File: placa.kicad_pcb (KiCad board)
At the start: 2 copper layers, 40 x 40 mm, 76 parts, among them J1 SW, J10 CONN_01X04_Straight, J12 CONN_01X04_Straight, J13 CONN_01X04_Straight, J14 CONN_01X04_Straight, J15 CONN_01X04_Straight, J16 CONN_01X04_Straight, J17 CONN_01X04_Straight, J18 CONN_01X06_Straight, J2 μUSB, J3 BATT, J5 CONN_01X04_Straight, J6 CONN_01X04_Straight, J7 CONN_02X12_Straight, J8 CONN_01X12_Straight, J9 CONN_01X04_Straight, Q1 FDC606P, Q2 BSS84, U1 AP2112K-3.3TRG1, U2 MCP73831, U3 MIC2253-06YML-TR, U4 ADS1000, U5 LMC7101AIM5, U6 DRV8837, U7 PCA9670, U8 DRV8837

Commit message: Schematic: Level shifter
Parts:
- removed J14, J15, J16, J17: CONN_01X04_Straight, Pin_Headers:Pin_Header_Straight_1x04_Pitch2.54mm
- removed J18: CONN_01X06_Straight, Pin_Headers:Pin_Header_Straight_1x06_Pitch2.54mm
- removed JP4: Jumper_NO, Connectors:GS2
- added Q3, Q4: BSS138P, TO_SOT_Packages_SMD:SOT-23, F.Cu at (168.5, 115.1)
- added R23, R24: 4.7k, Resistors_SMD:R_0402, F.Cu at (168.5, 115.1)
- D2: value BA340A -> LED; footprint Diodes_SMD:D_SMA -> LEDs:LED_0603
- D3: value LED -> BA340A; footprint LEDs:LED_0603 -> Diodes_SMD:D_SMA
- J11: value ~ -> CONN_01X04_Straight; footprint Connectors_Terminal_Blocks:TerminalBlock_Pheonix_MPT-2.54mm_2pol -> Pin_Headers:Pin_Header_Straight_1x04_Pitch2.54mm
- J5: value CONN_01X04_Straight -> ~; footprint Pin_Headers:Pin_Header_Straight_1x04_Pitch2.54mm -> Connectors_Terminal_Blocks:TerminalBlock_Pheonix_MPT-2.54mm_2pol
- J6: value CONN_01X04_Straight -> CONN_01X12_Straight; footprint Pin_Headers:Pin_Header_Straight_1x04_Pitch2.54mm -> Pin_Headers:Pin_Header_Straight_1x12_Pitch2.54mm
- J8: value CONN_01X12_Straight -> CONN_01X04_Straight; footprint Pin_Headers:Pin_Header_Straight_1x12_Pitch2.54mm -> Pin_Headers:Pin_Header_Straight_1x04_Pitch2.54mm
- R10: value 10k -> 620; footprint Resistors_SMD:R_0402 -> Resistors_SMD:R_0603
- R15: footprint Resistors_SMD:R_0603 -> Resistors_SMD:R_0402
- R16: value 0 -> 10k
- R17, R5: value 10k -> 0; footprint Resistors_SMD:R_0402 -> Resistors_SMD:R_0603
- R2: value 2k -> 330
- R20: value 4.7k -> 10k
- R21: value 330 -> 4.7k
- R3: value 30.9k -> 2k; footprint Resistors_SMD:R_0603 -> Resistors_SMD:R_0402
- R4: value 0 -> 30.9k
- R9: value 620 -> 10k; footprint Resistors_SMD:R_0603 -> Resistors_SMD:R_0402
- U7: value PCA9670 -> DRV8837; footprint alvaroferran:TSSOP-16 -> alvaroferran:WSON-8
- U8: value DRV8837 -> PCA9670; footprint alvaroferran:WSON-8 -> alvaroferran:TSSOP-16
- moved U8 82.9 mm to (172.2, 91.9), turned to 180 degrees
- moved J9 76.6 mm to (159.5, 77.0), turned to 180 degrees
- moved U6 50.5 mm to (179.3, 88.9), turned to 180 degrees
- moved J10 47.2 mm to (164.6, 77.0), turned to 180 degrees
- moved J5 37.4 mm to (185.2, 96.3), turned to 90 degrees
- moved J13 37.0 mm to (162.6, 98.0), turned to 180 degrees
- moved J12 36.8 mm to (159.8, 98.0), turned to 180 degrees
- moved J11 36.7 mm to (157.0, 98.0), turned to 180 degrees
- moved U7 28.1 mm to (179.3, 95.0), turned to 180 degrees
- moved J8 27.9 mm to (156.7, 77.0), turned to 180 degrees
- moved J3 22.9 mm to (170.2, 71.1)
- moved J6 20.2 mm to (182.5, 66.4), turned to 270 degrees
- moved J1 8.89 mm to (185.2, 80.0)
- moved J4 8.89 mm to (185.2, 90.2)
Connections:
- D1 pad 2: Net-(C5-Pad1) -> (no net)
- D2 pad 1: Net-(C7-Pad1) -> Net-(D2-Pad1)
- D2 pad 2: Net-(D2-Pad2) -> Net-(C5-Pad1)
- D3 pad 1: Net-(D3-Pad1) -> Net-(C7-Pad1)
- D3 pad 2: (no net) -> Net-(D3-Pad2)
- J10 pad 2: /UART2T -> /USB2+
- J10 pad 3: /UART2R -> /USB2-
- J11 pad 2: Net-(J11-Pad2) -> Net-(J11-Pad1)
- J12 pad 1: (no net) -> Net-(J12-Pad1)
- J12 pad 2: /SDA -> Net-(J12-Pad1)
- J12 pad 3: /SCL -> Net-(J12-Pad1)
- J12 pad 4: (no net) -> Net-(J12-Pad1)
- J13 pad 1: (no net) -> /GPIO0
- J13 pad 2: /SDA -> /GPIO1
- J13 pad 3: /SCL -> /GPIO2
- J13 pad 4: (no net) -> /GPIO3
- J5 pad 1: (no net) -> Net-(J5-Pad1)
- J5 pad 2: /USB1+ -> Net-(J5-Pad2)
- J6 pad 2: /USB2+ -> (no net)
- J6 pad 3: /USB2- -> (no net)
- J6 pad 4: (no net) -> /USB2+
- J7 pad 10: /UART1R -> (no net)
- J7 pad 11: /UART2T -> (no net)
- J7 pad 19: /MOSI -> (no net)
- J7 pad 21: /MISO -> (no net)
- J7 pad 22: /UART2R -> (no net)
- J7 pad 23: /SCK -> (no net)
- J7 pad 24: /CS -> (no net)
- J7 pad 8: /UART1T -> (no net)
- J8 pad 2: /USB1+ -> /SDA
- J8 pad 3: /USB1- -> /SCL
- J8 pad 4: /USB2+ -> (no net)
- J9 pad 2: /UART1T -> /SDA
- J9 pad 3: /UART1R -> /SCL
- L1 pad 2: Net-(D2-Pad2) -> Net-(D3-Pad2)
- R1 pad 1: Net-(R1-Pad1) -> (no net)
- R10 pad 1: Net-(R10-Pad1) -> Net-(C13-Pad1)
- R10 pad 2: (no net) -> Net-(R10-Pad2)
- R12 pad 1: /MOTEN -> Net-(R12-Pad1)
- R13 pad 1: Net-(R13-Pad1) -> /MOTEN
- R15 pad 1: Net-(C7-Pad2) -> Net-(R15-Pad1)
- R15 pad 2: GNDA -> (no net)
- R16 pad 1: (no net) -> Net-(C7-Pad2)
- R16 pad 2: GNDPWR -> GNDA
- R17 pad 1: Net-(JP1-Pad1) -> (no net)
- R17 pad 2: (no net) -> GNDPWR
- R18 pad 1: Net-(JP2-Pad1) -> Net-(JP1-Pad1)
- R19 pad 1: Net-(JP3-Pad1) -> Net-(JP2-Pad1)
- R2 pad 2: (no net) -> Net-(D2-Pad1)
- R20 pad 1: /SDA -> Net-(JP3-Pad1)
- R20 pad 2: Net-(JP4-Pad1) -> (no net)
- R21 pad 1: (no net) -> Net-(Q3-Pad1)
- R21 pad 2: Net-(D3-Pad1) -> /SDA
- R22 pad 1: /SCL -> (no net)
- R22 pad 2: Net-(JP4-Pad1) -> /SDAH
- R3 pad 1: Net-(C7-Pad1) -> Net-(R3-Pad1)
- R3 pad 2: Net-(C7-Pad2) -> (no net)
- R4 pad 1: (no net) -> Net-(C7-Pad1)
- R4 pad 2: GNDA -> Net-(C7-Pad2)
- R5 pad 2: Net-(R10-Pad1) -> GNDA
- R7 pad 2: Net-(R13-Pad1) -> Net-(R12-Pad1)
- R9 pad 1: Net-(C13-Pad1) -> (no net)
- R9 pad 2: Net-(R9-Pad2) -> Net-(R15-Pad1)
- U2 pad 1: Net-(R1-Pad1) -> Net-(R2-Pad1)
- U2 pad 5: Net-(R2-Pad1) -> Net-(R3-Pad1)
- U3 pad 12: Net-(R9-Pad2) -> Net-(R10-Pad2)
- U3 pad 7: Net-(D2-Pad2) -> Net-(D3-Pad2)
- U3 pad 8: Net-(D2-Pad2) -> Net-(D3-Pad2)
- U4 pad 1: Net-(R14-Pad1) -> Net-(R15-Pad1)
- U4 pad 6: Net-(R13-Pad1) -> Net-(R14-Pad1)
- U5 pad 3: Net-(R10-Pad1) -> Net-(R11-Pad1)
- U5 pad 4: Net-(R11-Pad1) -> Net-(R12-Pad1)
- U7 pad 1: Net-(JP3-Pad1) -> (no net)
- U7 pad 2: /GPIO0 -> Net-(J5-Pad1)
- U7 pad 3: /GPIO1 -> Net-(J5-Pad2)
- U7 pad 4: /GPIO2 -> (no net)
- U7 pad 5: /GPIO3 -> /MOT2B
- U7 pad 6: (no net) -> /MOT2A
- U7 pad 7: /MOT1A -> /MOTEN
- U7 pad 8: /MOT1B -> (no net)
- U7 pad 9: /MOT2A -> (no net)
- U8 pad 1: (no net) -> Net-(JP3-Pad1)
- U8 pad 2: Net-(J11-Pad1) -> /GPIO0
- U8 pad 3: Net-(J11-Pad2) -> /GPIO1
- U8 pad 4: (no net) -> /GPIO2
- U8 pad 5: /MOT2B -> /GPIO3
- U8 pad 6: /MOT2A -> (no net)
- U8 pad 7: /MOTEN -> /MOT1A
- U8 pad 8: (no net) -> /MOT1B
- U8 pad 9: (no net) -> /MOT2A

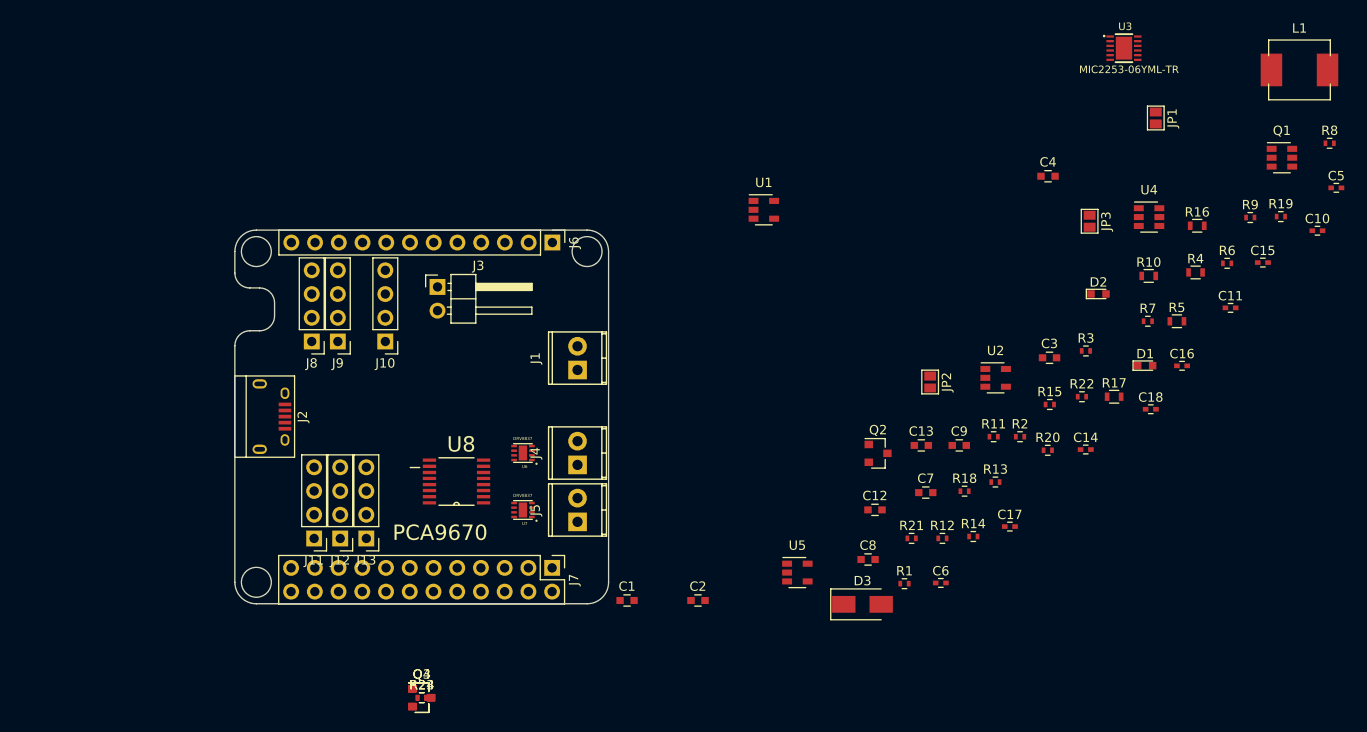
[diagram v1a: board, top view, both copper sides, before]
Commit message: Schematic: Protection diode
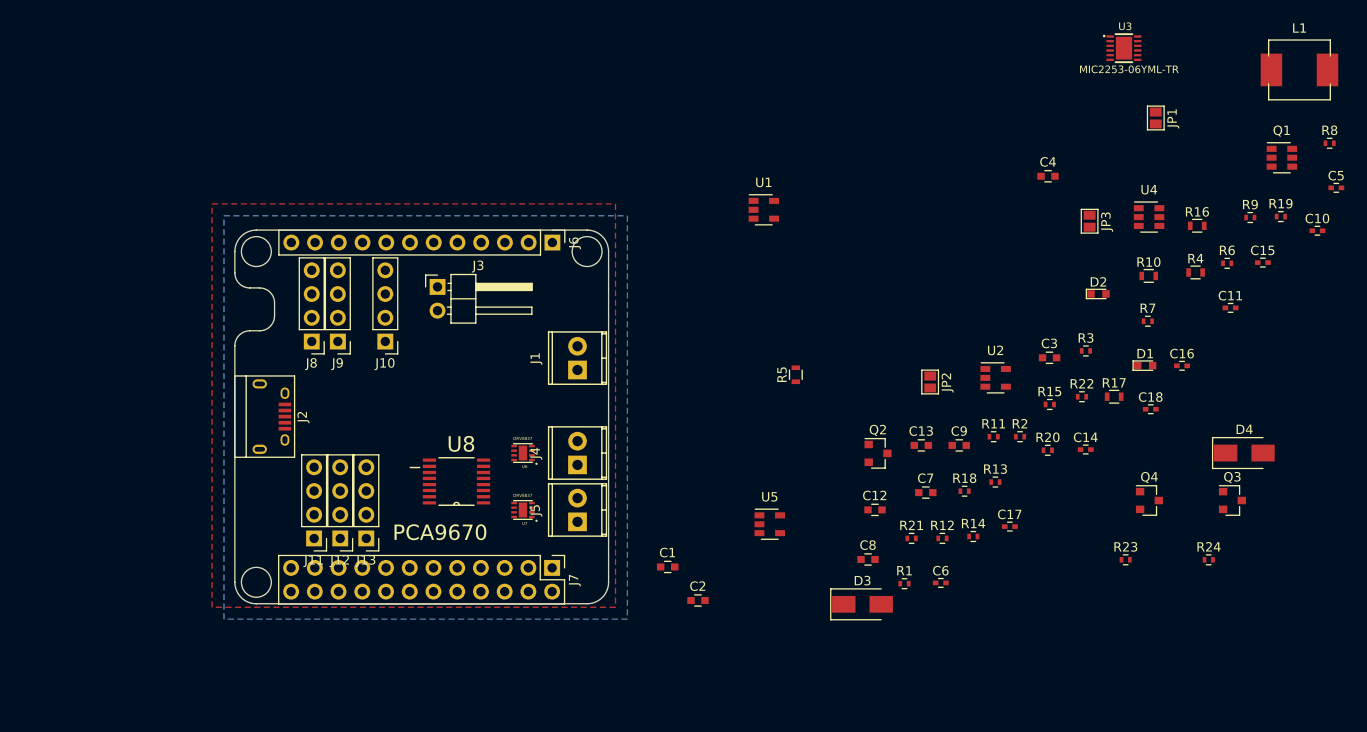
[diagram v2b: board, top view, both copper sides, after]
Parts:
- added D4: BA340A, Diodes_SMD:D_SMA, F.Cu at (256.5, 88.9)
- R16: value 10k -> 0
- R17: value 0 -> 10k
- R4: value 30.9k -> 0
- R5: value 0 -> 30.9k
- moved Q3 89.3 mm to (255.3, 94.0)
- moved R24 85.5 mm to (252.7, 100.3)
- moved Q4 80.7 mm to (246.4, 94.0)
- moved R23 76.8 mm to (243.8, 100.3)
- moved R5 41.2 mm to (208.5, 80.5), turned to 90 degrees
- moved U5 5.96 mm to (205.7, 96.5)
- moved C1 5.64 mm to (194.8, 101.1)
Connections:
- C1 pad 1: (no net) -> 5V
- C1 pad 2: (no net) -> GND
- C10 pad 1: (no net) -> 3.3V
- C10 pad 2: (no net) -> GND
- C11 pad 1: (no net) -> 3.3V
- C11 pad 2: (no net) -> GND
- C14 pad 1: (no net) -> 3.3V
- C14 pad 2: (no net) -> GND
- C15 pad 1: (no net) -> 5V
- C15 pad 2: (no net) -> GND
- C16 pad 1: (no net) -> 3.3V
- C16 pad 2: (no net) -> GND
- C17 pad 1: (no net) -> 5V
- C17 pad 2: (no net) -> GND
- C18 pad 1: (no net) -> 5V
- C18 pad 2: (no net) -> GND
- C2 pad 1: (no net) -> 3.3V
- C2 pad 2: (no net) -> GND
- C3 pad 1: Net-(C3-Pad1) -> 5V
- C3 pad 2: Net-(C3-Pad2) -> GND
- C4 pad 1: Net-(C4-Pad1) -> 3.3V
- C4 pad 2: Net-(C3-Pad2) -> GND
- C5 pad 2: (no net) -> GND
- C6 pad 2: (no net) -> GND
- C7 pad 1: Net-(C7-Pad1) -> 5V
- C8 pad 1: Net-(C8-Pad1) -> VBAT
- C9 pad 1: Net-(C7-Pad1) -> 5V
- D1 pad 2: (no net) -> 3.3V
- D3 pad 1: Net-(C7-Pad1) -> 5V
- J1 pad 1: (no net) -> VBAT
- J10 pad 1: (no net) -> 5V
- J10 pad 4: (no net) -> GND
- J11 pad 1: Net-(J11-Pad1) -> GND
- J11 pad 2: Net-(J11-Pad1) -> GND
- J11 pad 3: Net-(J11-Pad1) -> GND
- J11 pad 4: Net-(J11-Pad1) -> GND
- J12 pad 1: Net-(J12-Pad1) -> 5V
- J12 pad 2: Net-(J12-Pad1) -> 5V
- J12 pad 3: Net-(J12-Pad1) -> 5V
- J12 pad 4: Net-(J12-Pad1) -> 5V
- J2 pad 5: (no net) -> GND
- J3 pad 2: (no net) -> GND
- J6 pad 12: (no net) -> GND
- J7 pad 14: Net-(J7-Pad14) -> GND
- J7 pad 20: Net-(J7-Pad14) -> GND
- J7 pad 6: Net-(J7-Pad14) -> GND
- J7 pad 9: (no net) -> GND
- J8 pad 1: (no net) -> 3.3V
- J8 pad 4: (no net) -> GND
- J9 pad 1: (no net) -> 3.3V
- J9 pad 4: (no net) -> GND
- JP1 pad 2: Net-(JP1-Pad2) -> 5V
- JP2 pad 2: Net-(JP1-Pad2) -> 5V
- JP3 pad 2: Net-(JP1-Pad2) -> 5V
- L1 pad 1: Net-(C8-Pad1) -> VBAT
- Q1 pad 3: Net-(J3-Pad1) -> GND
- Q2 pad 2: (no net) -> 3.3V
- Q3 pad 1: Net-(Q3-Pad1) -> 3.3V
- Q4 pad 1: Net-(Q4-Pad1) -> 3.3V
- R1 pad 1: (no net) -> GND
- R11 pad 2: (no net) -> GND
- R12 pad 2: (no net) -> GND
- R13 pad 2: (no net) -> GND
- R14 pad 2: (no net) -> GND
- R15 pad 2: (no net) -> GND
- R16 pad 1: Net-(C7-Pad2) -> GND
- R16 pad 2: GNDA -> GNDPWR
- R17 pad 1: (no net) -> Net-(C7-Pad2)
- R17 pad 2: GNDPWR -> GNDA
- R18 pad 2: (no net) -> GND
- R19 pad 2: (no net) -> GND
- R20 pad 2: (no net) -> GND
- R21 pad 1: Net-(Q3-Pad1) -> 3.3V
- R22 pad 1: (no net) -> 5V
- R23 pad 1: Net-(Q4-Pad1) -> 3.3V
- R24 pad 1: (no net) -> 5V
- R3 pad 2: (no net) -> GND
- R4 pad 1: Net-(C7-Pad1) -> GND
- R4 pad 2: Net-(C7-Pad2) -> GNDA
- R5 pad 1: (no net) -> 5V
- R5 pad 2: GNDA -> Net-(C7-Pad2)
- R6 pad 1: (no net) -> 3.3V
- R7 pad 1: (no net) -> VBAT
- R8 pad 1: (no net) -> VBAT
- R9 pad 1: (no net) -> 3.3V
- U1 pad 1: Net-(C3-Pad1) -> 5V
- U1 pad 2: Net-(C3-Pad2) -> GND
- U1 pad 3: Net-(C3-Pad1) -> 5V
- U1 pad 5: Net-(C4-Pad1) -> 3.3V
- U2 pad 2: (no net) -> GND
- U3 pad 10: Net-(C8-Pad1) -> VBAT
- U3 pad 11: Net-(C8-Pad1) -> VBAT
- U3 pad 9: Net-(C7-Pad1) -> 5V
- U4 pad 2: (no net) -> GND
- U4 pad 5: (no net) -> 3.3V
- U5 pad 2: (no net) -> 3.3V
- U5 pad 5: (no net) -> GND
- U6 pad 1: (no net) -> 5V
- U6 pad 4: (no net) -> GND
- U6 pad 8: (no net) -> 3.3V
- U7 pad 1: (no net) -> 5V
- U7 pad 4: (no net) -> GND
- U7 pad 8: (no net) -> 3.3V
- U8 pad 11: Net-(JP1-Pad2) -> 5V
- U8 pad 14: Net-(JP1-Pad2) -> 5V
- U8 pad 6: (no net) -> GND
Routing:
- added copper zone on B.Cu, net GND
- added copper zone on F.Cu, net GND

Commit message: Schematic: Batt inv removed
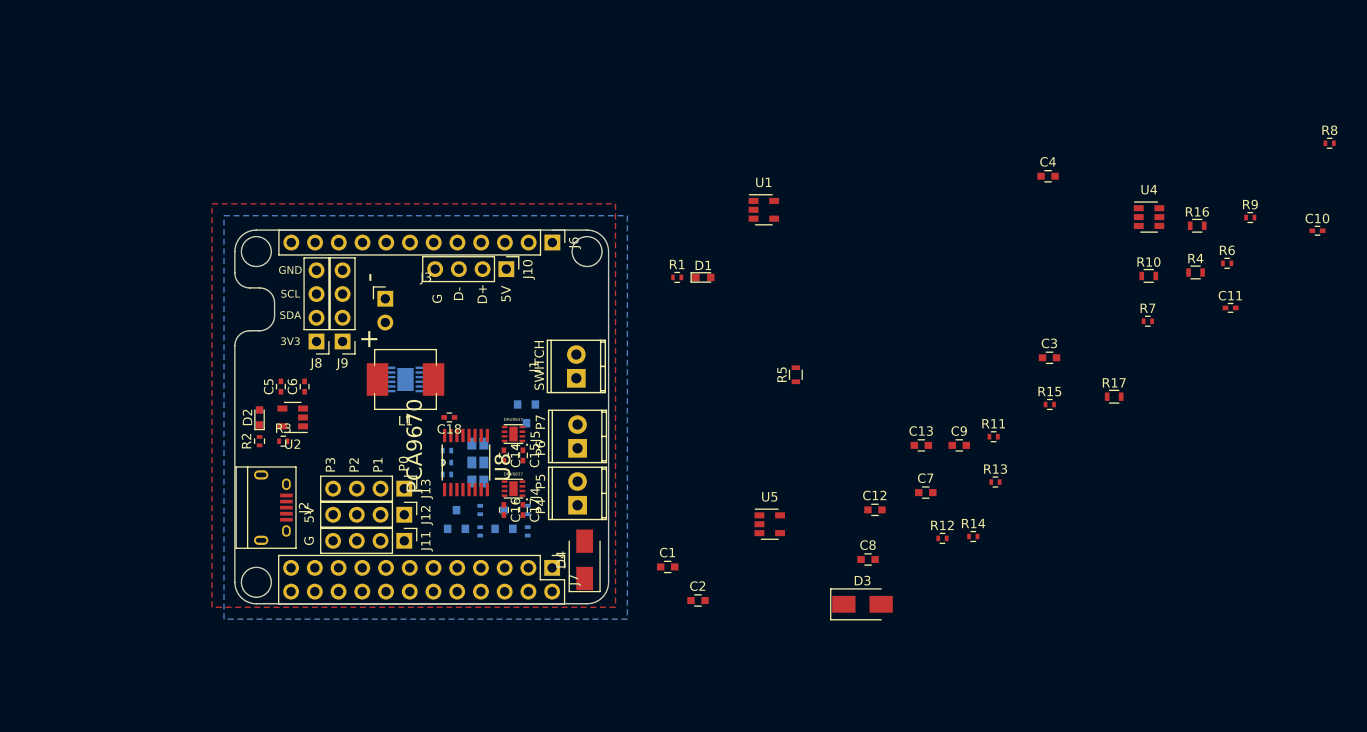
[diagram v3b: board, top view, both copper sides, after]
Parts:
- removed Q4: BSS138P, TO_SOT_Packages_SMD:SOT-23
- JP1, JP2, JP3, Q3, R18, R19, R20, R21, R22, R23, R24, U3: moved to B.Cu
- Q1: value FDC606P -> BSS84; footprint TO_SOT_Packages_SMD:SOT-23-6 -> TO_SOT_Packages_SMD:SOT-23; moved to B.Cu
- Q2: value BSS84 -> BSS138P; moved to B.Cu
- moved C5 115.0 mm to (153.4, 81.8), turned to 90 degrees
- moved L1 101.3 mm to (166.8, 81.0), turned to 180 degrees
- moved R19 93.0 mm to (171.2, 89.9), turned to 180 degrees
- moved D2 90.8 mm to (151.1, 85.1), turned to 90 degrees
- moved R3 86.5 mm to (153.7, 87.6)
- moved Q1 85.4 mm to (179.7, 84.7), turned to 270 degrees
- moved U3 84.7 mm to (166.8, 81.0)
- moved C15 81.8 mm to (179.3, 89.2), turned to 270 degrees
- moved R2 81.4 mm to (151.1, 87.6), turned to 90 degrees
- moved JP1 80.5 mm to (174.5, 87.9), turned to 270 degrees
- moved Q3 78.0 mm to (177.3, 96.0), turned to 90 degrees
- moved U2 75.3 mm to (154.7, 85.1), turned to 180 degrees
- moved C18 75.1 mm to (171.4, 85.1), turned to 180 degrees
- moved C16 74.2 mm to (177.3, 95.0), turned to 270 degrees
- moved R24 73.1 mm to (179.8, 95.0), turned to 270 degrees
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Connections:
- J3 pad 1: Net-(J3-Pad1) -> GND
- J3 pad 2: GND -> Net-(C6-Pad1)
- Q1 pad 1: Net-(J3-Pad1) -> Net-(Q1-Pad1)
- Q1 pad 2: Net-(J3-Pad1) -> 3.3V
- Q1 pad 3: GND -> /MOTEN
- Q2 pad 1: Net-(Q2-Pad1) -> 3.3V
- Q2 pad 2: 3.3V -> /SDA
- Q2 pad 3: /MOTEN -> /SDAH
- Q3 pad 2: /SDA -> /SCL
- Q3 pad 3: /SDAH -> /SCLH
- U5 pad 1: Net-(Q2-Pad1) -> Net-(Q1-Pad1)
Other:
- board text added: "+"
- board text added: "-"
- board text added: "3V3"
- board text added: "5V"
- board text added: "CHANGE BAT CONNECTOR ADD STRESS RELIEF FOR WIRES"
- board text added: "D+"
- board text added: "D-"
- board text added: "G"
- board text added: "GND"
- board text added: "P0"
- board text added: "P1"
- board text added: "P2"
- board text added: "P3"
- board text added: "P4"
- board text added: "P5"
- board text added: "P6"
- board text added: "P7"
- board text added: "SCL"
- board text added: "SDA"
- board text added: "SWITCH"

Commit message: Board: components in place
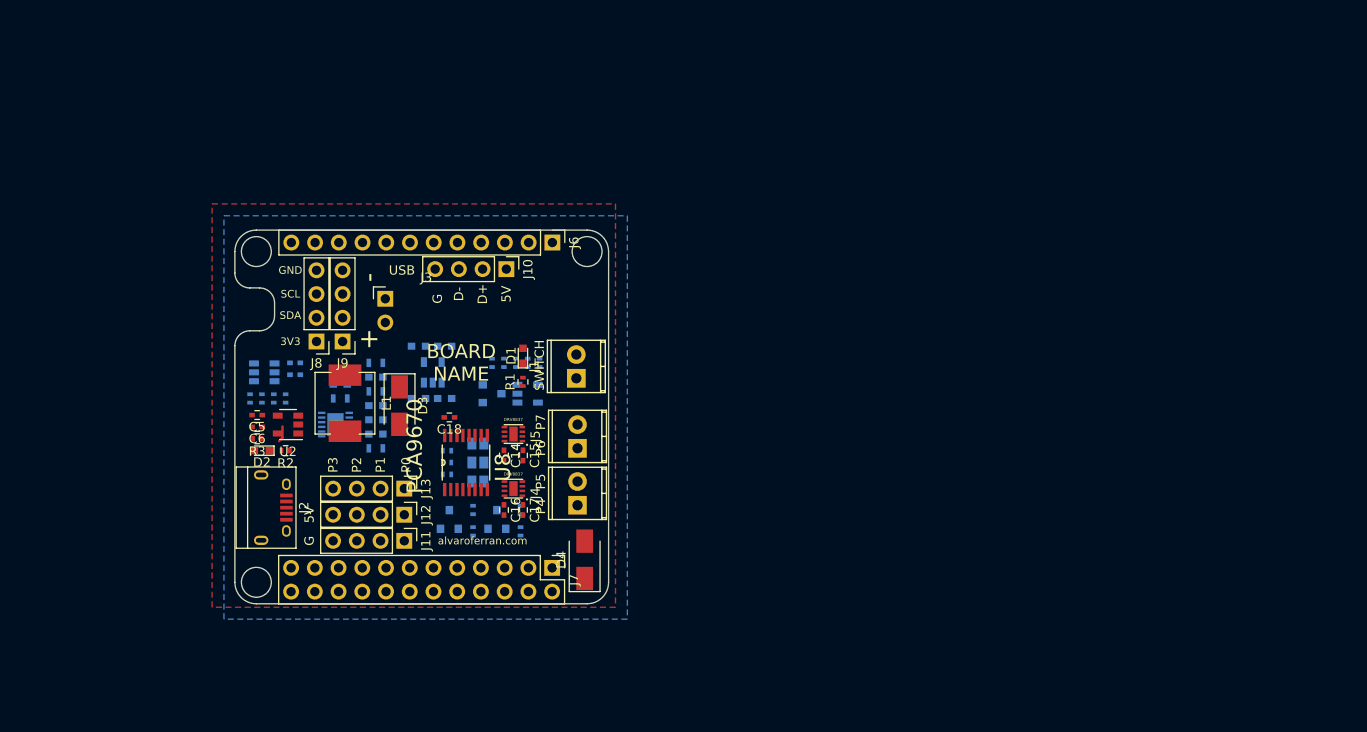
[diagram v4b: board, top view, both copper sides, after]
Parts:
- C1, C10, C11, C12, C13, C2, C3, C4, C7, C8, C9, R10, R11, R12, R13, R14, R15, R16, R17, R4, R5, R6, R7, R8, R9, U1, U4, U5: moved to B.Cu
- moved R8 115.0 mm to (153.9, 83.1), turned to 90 degrees
- moved C10 110.5 mm to (154.9, 80.5)
- moved R9 107.5 mm to (151.4, 83.1), turned to 90 degrees
- moved C11 100.3 mm to (154.9, 79.2)
- moved U4 96.2 mm to (151.6, 80.3)
- moved R16 91.1 mm to (163.6, 88.4), turned to 180 degrees
- moved R4 88.3 mm to (163.6, 79.2)
- moved R10 87.1 mm to (159.8, 80.0), turned to 180 degrees
- moved R15 85.6 mm to (150.1, 83.1), turned to 270 degrees
- moved R17 79.0 mm to (163.6, 82.3)
- moved R6 78.1 mm to (177.3, 79.2), turned to 270 degrees
- moved R14 76.3 mm to (152.7, 83.1), turned to 270 degrees
- moved C4 67.1 mm to (170.9, 77.5)
- moved R7 65.3 mm to (181.1, 79.2), turned to 270 degrees
- moved C3 64.9 mm to (170.9, 83.1)
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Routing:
- net (no net): track 0.00 -> 1.74 mm
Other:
- board text added: "AD0"
- board text added: "AD1"
- board text added: "AD2"
- board text added: "Alvaro Ferrán"
- board text added: "BATT STRESS RELIEF"
- board text added: "BOARD NAME"
- board text added: "USB"
- board text added: "alvaroferran.com"
- board text removed: "CHANGE BAT CONNECTOR ADD STRESS RELIEF FOR WIRES"
